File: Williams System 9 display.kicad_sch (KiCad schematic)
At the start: 30 parts, among them J101 Conn_01x02, J102 Conn_01x08, J103 Conn_01x08, J104 Conn_01x03, J105 Conn_01x04, J106 Conn_01x04, U101 74HC148, U102 74LV08A, U103 Pico, U104 74HC148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

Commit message: Make AKL available via personal component library for ease of integration
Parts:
- C101, C102, C103, C104, C105, C106, C107, C108: symbol PCM_Capacitor_US_AKL:C_0805 -> Capacitor_US_AKL:C_0805
- R101, R102, R103, R104, R105: symbol PCM_Resistor_US_AKL:R_0805 -> Resistor_US_AKL:R_0805
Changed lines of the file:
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@@
     )
   )
-  (symbol (lib_id "PCM_Capacitor_US_AKL:C_0805") (at 256.54 127 0) (unit 1)
+  (symbol (lib_id "Capacitor_US_AKL:C_0805") (at 256.54 127 0) (unit 1)
     (in_bom yes) (on_board yes) (dnp no) (fields_autoplaced)
     (property "Reference" "C108" (at 260.35 125.73 0)
@@
     )
   )
-  (symbol (lib_id "PCM_Resistor_US_AKL:R_0805") (at 255.27 90.17 0) (unit 1)
+  (symbol (lib_id "Resistor_US_AKL:R_0805") (at 255.27 90.17 0) (unit 1)
     (in_bom yes) (on_board yes) (dnp no)
     (property "Reference" "R102" (at 256.54 88.9 0)
@@
     )
   )
-  (symbol (lib_id "PCM_Capacitor_US_AKL:C_0805") (at 203.2 133.35 0) (mirror y) (unit 1)
+  (symbol (lib_id "Capacitor_US_AKL:C_0805") (at 203.2 133.35 0) (mirror y) (unit 1)
     (in_bom yes) (on_board yes) (dnp no)
     (property "Reference" "C107" (at 199.39 132.08 0)
@@
     )
   )
-  (symbol (lib_id "PCM_Resistor_US_AKL:R_0805") (at 257.81 64.77 90) (unit 1)
+  (symbol (lib_id "Resistor_US_AKL:R_0805") (at 257.81 64.77 90) (unit 1)
     (in_bom yes) (on_board yes) (dnp no)
     (property "Reference" "R105" (at 257.81 59.69 90)
@@
     )
   )
-  (symbol (lib_id "PCM_Capacitor_US_AKL:C_0805") (at 127 30.48 0) (unit 1)
+  (symbol (lib_id "Capacitor_US_AKL:C_0805") (at 127 30.48 0) (unit 1)
     (in_bom yes) (on_board yes) (dnp no)
     (property "Reference" "C102" (at 129.54 29.21 0)
@@
     )
   )
-  (symbol (lib_id "PCM_Resistor_US_AKL:R_0805") (at 257.81 73.66 90) (unit 1)
+  (symbol (lib_id "Resistor_US_AKL:R_0805") (at 257.81 73.66 90) (unit 1)
     (in_bom yes) (on_board yes) (dnp no)
     (property "Reference" "R104" (at 257.81 68.58 90)
@@
     )
   )
-  (symbol (lib_id "PCM_Capacitor_US_AKL:C_0805") (at 66.04 82.55 0) (unit 1)
+  (symbol (lib_id "Capacitor_US_AKL:C_0805") (at 66.04 82.55 0) (unit 1)
     (in_bom yes) (on_board yes) (dnp no)
     (property "Reference" "C103" (at 68.58 81.28 0)
@@
     )
   )
-  (symbol (lib_id "PCM_Capacitor_US_AKL:C_0805") (at 66.04 27.94 0) (unit 1)
+  (symbol (lib_id "Capacitor_US_AKL:C_0805") (at 66.04 27.94 0) (unit 1)
     (in_bom yes) (on_board yes) (dnp no)
     (property "Reference" "C101" (at 68.58 26.67 0)
@@
     )
   )
-  (symbol (lib_id "PCM_Capacitor_US_AKL:C_0805") (at 81.28 154.94 0) (unit 1)
+  (symbol (lib_id "Capacitor_US_AKL:C_0805") (at 81.28 154.94 0) (unit 1)
     (in_bom yes) (on_board yes) (dnp no) (fields_autoplaced)
     (property "Reference" "C106" (at 85.09 153.67 0)
@@
     )
   )
-  (symbol (lib_id "PCM_Capacitor_US_AKL:C_0805") (at 115.57 121.92 0) (unit 1)
+  (symbol (lib_id "Capacitor_US_AKL:C_0805") (at 115.57 121.92 0) (unit 1)
     (in_bom yes) (on_board yes) (dnp no)
     (property "Reference" "C104" (at 118.11 120.65 0)
@@
     )
   )
-  (symbol (lib_id "PCM_Resistor_US_AKL:R_0805") (at 257.81 78.74 90) (unit 1)
+  (symbol (lib_id "Resistor_US_AKL:R_0805") (at 257.81 78.74 90) (unit 1)
     (in_bom yes) (on_board yes) (dnp no)
     (property "Reference" "R103" (at 257.81 81.28 90)
@@
     )
   )
-  (symbol (lib_id "PCM_Resistor_US_AKL:R_0805") (at 264.16 93.98 0) (unit 1)
+  (symbol (lib_id "Resistor_US_AKL:R_0805") (at 264.16 93.98 0) (unit 1)
     (in_bom yes) (on_board yes) (dnp no)
     (property "Reference" "R101" (at 265.43 92.71 0)
@@
     )
   )
-  (symbol (lib_id "PCM_Capacitor_US_AKL:C_0805") (at 154.94 153.67 0) (unit 1)
+  (symbol (lib_id "Capacitor_US_AKL:C_0805") (at 154.94 153.67 0) (unit 1)
     (in_bom yes) (on_board yes) (dnp no) (fields_autoplaced)
     (property "Reference" "C105" (at 158.75 152.4 0)

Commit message: Address the remaining ERC violations
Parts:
- U107: footprint Package_TO_SOT_SMD_AKL:SOT-363_SC-70-6_BigPads -> Package_TO_SOT_SMD_AKL:SOT-363_SC-70-6_Handsoldering
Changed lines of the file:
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@@
   (junction (at 154.94 158.75) (diameter 0) (color 0 0 0 0)
+  )
+  (junction (at 130.81 25.4) (diameter 0) (color 0 0 0 0)
   )
   (junction (at 139.7 35.56) (diameter 0) (color 0 0 0 0)
@@
   (no_connect (at 223.52 104.14))
   (no_connect (at 143.51 173.99))
-  (wire (pts (xy 127 25.4) (xy 135.89 25.4))
+  (wire (pts (xy 127 25.4) (xy 130.81 25.4))
     (stroke (width 0) (type default))
   )
@@
   )
   (wire (pts (xy 123.19 27.94) (xy 123.19 35.56))
+    (stroke (width 0) (type default))
+  )
+  (wire (pts (xy 130.81 25.4) (xy 135.89 25.4))
     (stroke (width 0) (type default))
   )
@@
       (effects (font (size 1.27 1.27)))
     )
-    (property "Footprint" "Package_TO_SOT_SMD_AKL:SOT-363_SC-70-6_BigPads" (at 146.05 39.37 0)
+    (property "Footprint" "Package_TO_SOT_SMD_AKL:SOT-363_SC-70-6_Handsoldering" (at 146.05 39.37 0)
       (effects (font (size 1.27 1.27)) hide)
     )
@@
     (pin "2")
     (pin "3")
-    (pin "5")
     (pin "6")
     (pin "4")
+    (pin "5" (alternate "ST_{NA}"))
     (instances
       (project "Williams System 9 display"
@@
         )
       )
+    )
+  )
+  (symbol (lib_id "power:PWR_FLAG") (at 130.81 25.4 0) (unit 1)
+    (in_bom yes) (on_board yes) (dnp no) (fields_autoplaced)
+    (property "Reference" "#FLG0101" (at 130.81 23.495 0)
+      (effects (font (size 1.27 1.27)) hide)
+    )
+    (property "Value" "PWR_FLAG" (at 130.81 20.32 0)
+      (effects (font (size 1.27 1.27)) hide)
+    )
+    (property "Footprint" "" (at 130.81 25.4 0)
+      (effects (font (size 1.27 1.27)) hide)
+    )
+    (property "Datasheet" "~" (at 130.81 25.4 0)
+      (effects (font (size 1.27 1.27)) hide)
+    )
+    (pin "1")
+    (instances
+      (project "Williams System 9 display"
+        (path "/4315ddb4-8ca0-4300-a1f0-a77c526acaa2"
+          (reference "#FLG0101") (unit 1)
+        )
+      )

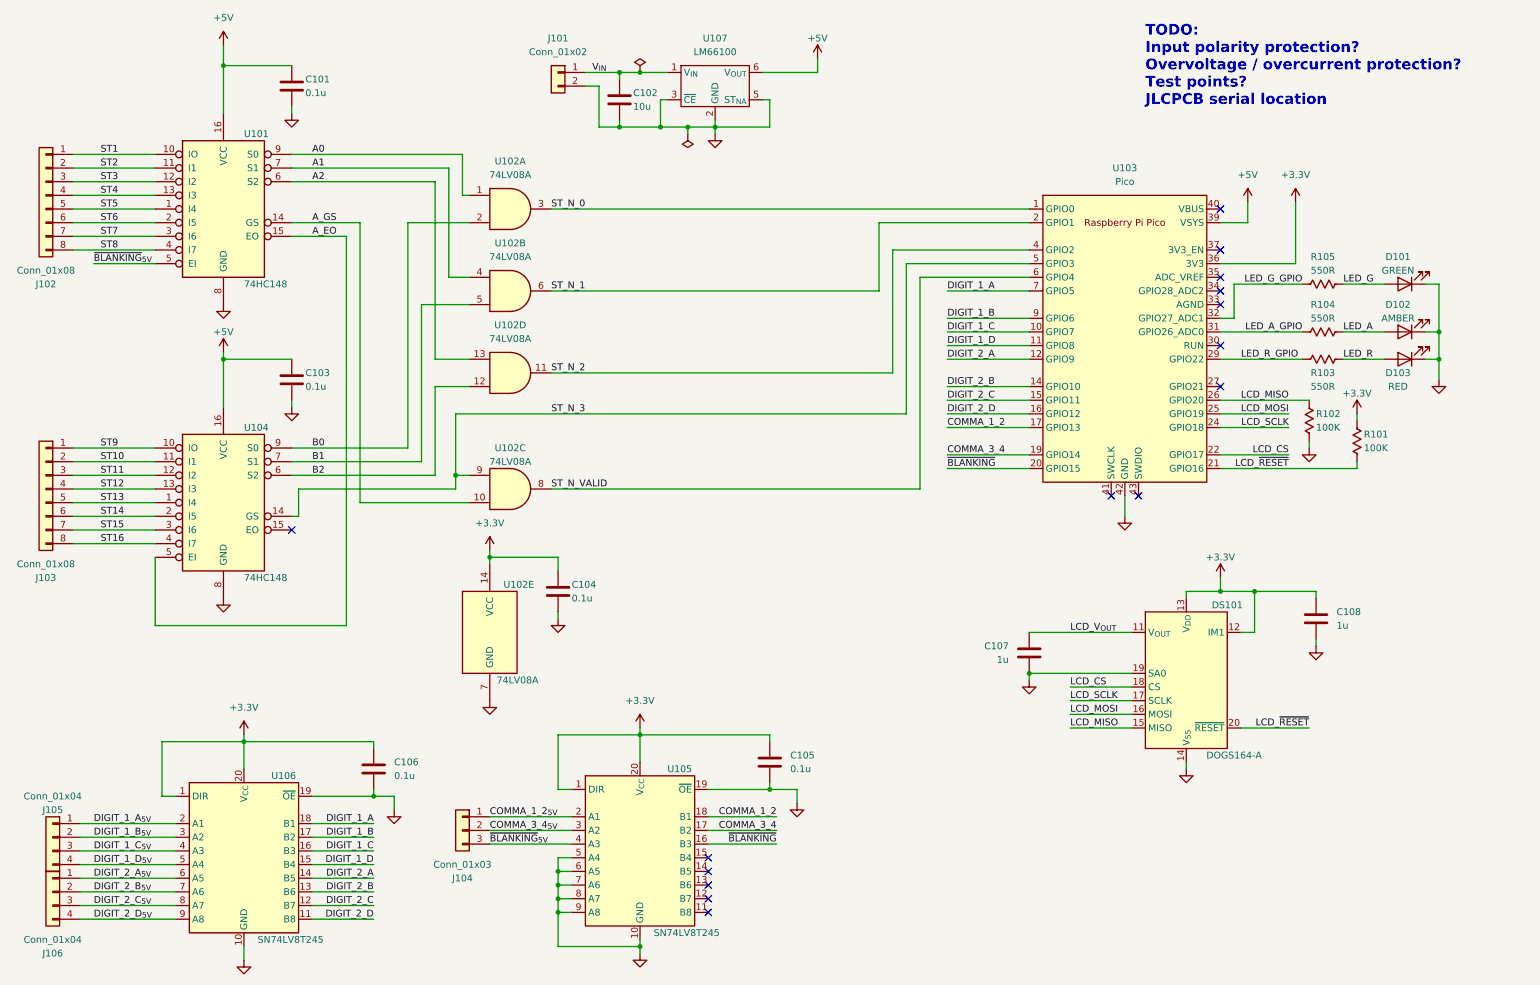
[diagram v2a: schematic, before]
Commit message: More informative silkscreen
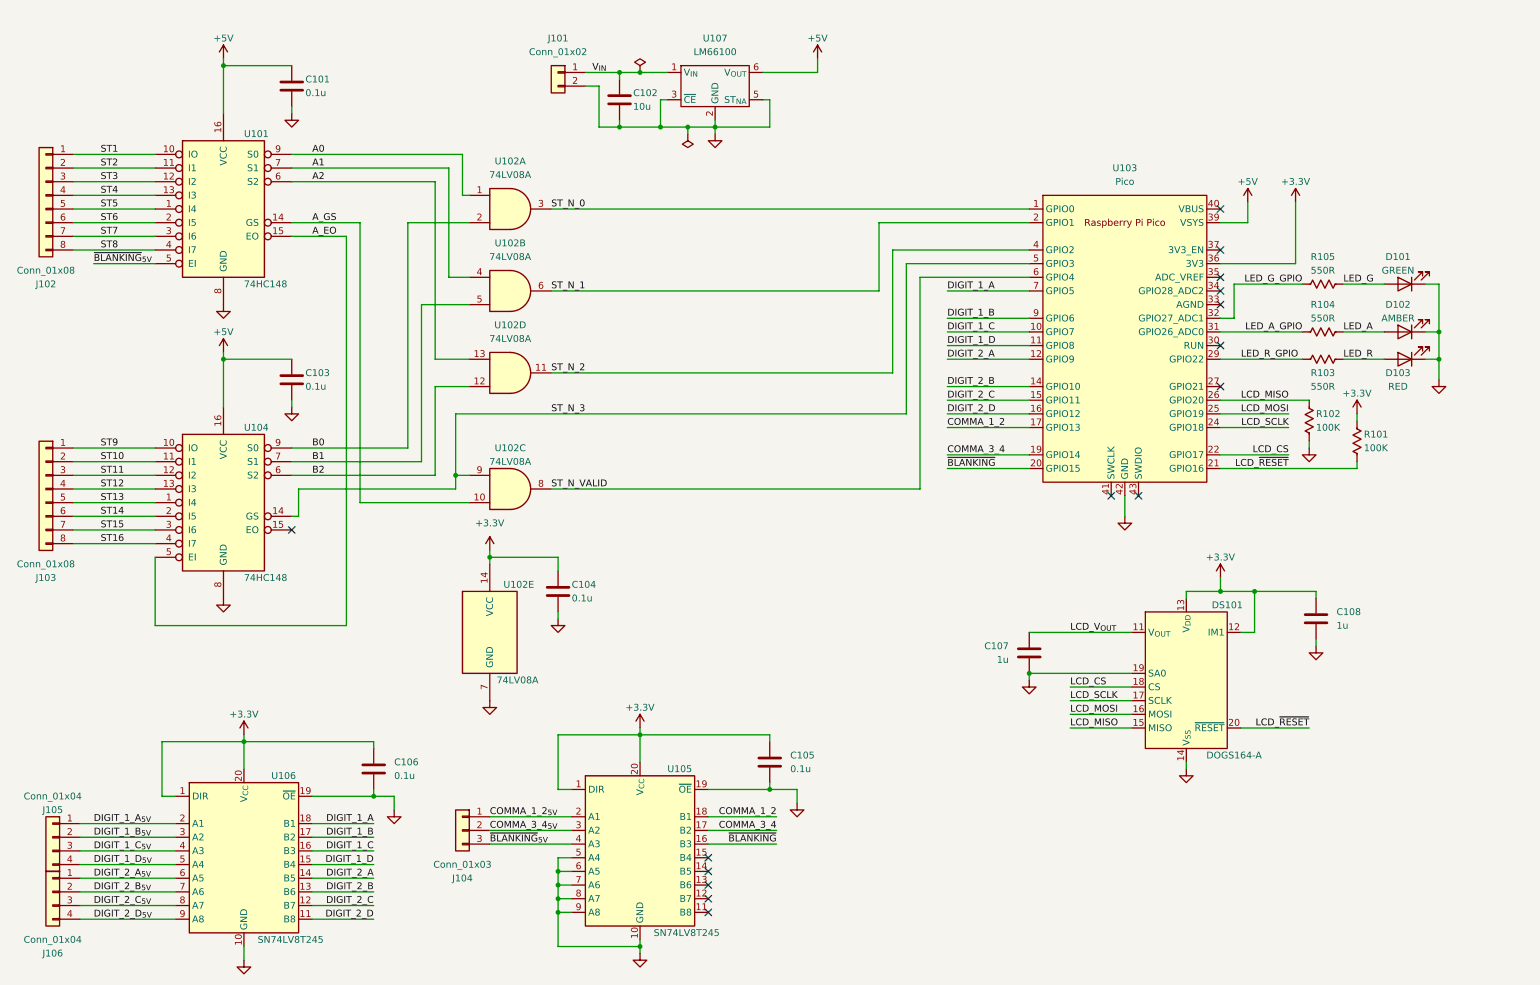
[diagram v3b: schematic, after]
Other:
- note removed: "TODO: Input polarity protection? Overvoltage / overcurrent protection? Test points? JLCPCB serial location"
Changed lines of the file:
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@@
     (stroke (width 0) (type default))
   )
-  (wire (pts (xy 53.34 20.32) (xy 53.34 24.13))
+  (wire (pts (xy 53.34 22.86) (xy 53.34 24.13))
     (stroke (width 0) (type default))
   )
@@
   (wire (pts (xy 90.17 97.79) (xy 90.17 68.58))
     (stroke (width 0) (type default))
-  )
-  (text "TODO:\nInput polarity protection?\nOvervoltage / overcurrent protection?\nTest points?\nJLCPCB serial location"
-    (at 224.79 31.75 0)
-    (effects (font (size 2 2) (thickness 0.4) bold) (justify left bottom))
   )
   (label "ST_N_0" (at 114.3 50.8 0) (fields_autoplaced)
@@
   )
   (symbol (lib_id "power:+3.3V") (at 130.81 147.32 0) (unit 1)
-    (in_bom yes) (on_board yes) (dnp no) (fields_autoplaced)
+    (in_bom yes) (on_board yes) (dnp no)
     (property "Reference" "#PWR0115" (at 130.81 151.13 0)
       (effects (font (size 1.27 1.27)) hide)
     )
-    (property "Value" "+3.3V" (at 130.81 142.24 0)
+    (property "Value" "+3.3V" (at 130.81 143.51 0)
       (effects (font (size 1.27 1.27)))
     )
@@
     )
   )
-  (symbol (lib_id "power:+5V") (at 53.34 20.32 0) (unit 1)
-    (in_bom yes) (on_board yes) (dnp no) (fields_autoplaced)
-    (property "Reference" "#PWR0101" (at 53.34 24.13 0)
-      (effects (font (size 1.27 1.27)) hide)
-    )
-    (property "Value" "+5V" (at 53.34 15.24 0)
-      (effects (font (size 1.27 1.27)))
-    )
-    (property "Footprint" "" (at 53.34 20.32 0)
-      (effects (font (size 1.27 1.27)) hide)
-    )
-    (property "Datasheet" "" (at 53.34 20.32 0)
+  (symbol (lib_id "power:+5V") (at 53.34 22.86 0) (unit 1)
+    (in_bom yes) (on_board yes) (dnp no)
+    (property "Reference" "#PWR0101" (at 53.34 26.67 0)
+      (effects (font (size 1.27 1.27)) hide)
+    )
+    (property "Value" "+5V" (at 53.34 19.05 0)
+      (effects (font (size 1.27 1.27)))
+    )
+    (property "Footprint" "" (at 53.34 22.86 0)
+      (effects (font (size 1.27 1.27)) hide)
+    )
+    (property "Datasheet" "" (at 53.34 22.86 0)
       (effects (font (size 1.27 1.27)) hide)
     )
@@
   )
   (symbol (lib_id "power:+5V") (at 243.84 49.53 0) (unit 1)
-    (in_bom yes) (on_board yes) (dnp no) (fields_autoplaced)
+    (in_bom yes) (on_board yes) (dnp no)
     (property "Reference" "#PWR0105" (at 243.84 53.34 0)
       (effects (font (size 1.27 1.27)) hide)
     )
-    (property "Value" "+5V" (at 243.84 44.45 0)
+    (property "Value" "+5V" (at 243.84 45.72 0)
       (effects (font (size 1.27 1.27)))
     )
@@
   )
   (symbol (lib_id "power:+3.3V") (at 252.73 49.53 0) (unit 1)
-    (in_bom yes) (on_board yes) (dnp no) (fields_autoplaced)
+    (in_bom yes) (on_board yes) (dnp no)
     (property "Reference" "#PWR0106" (at 252.73 53.34 0)
       (effects (font (size 1.27 1.27)) hide)
     )
-    (property "Value" "+3.3V" (at 252.73 44.45 0)
+    (property "Value" "+3.3V" (at 252.73 45.72 0)
       (effects (font (size 1.27 1.27)))
     )
@@
   )
   (symbol (lib_id "power:+3.3V") (at 57.15 148.59 0) (unit 1)
-    (in_bom yes) (on_board yes) (dnp no) (fields_autoplaced)
+    (in_bom yes) (on_board yes) (dnp no)
     (property "Reference" "#PWR0116" (at 57.15 152.4 0)
       (effects (font (size 1.27 1.27)) hide)
     )
-    (property "Value" "+3.3V" (at 57.15 143.51 0)
-      (effects (font (size 1.27 1.27)))
-    )
+    (property "Value" "+3.3V" (at 57.15 144.78 0)
+      (effects (font (size 1.27 1.27)))
+    )

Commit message: Don't use BLANKING as enable signal for priority encoder since it is of the wrong polarity
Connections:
- net GND: now also U101.5 (EI)
- net ~{BLANKING}_{5V}: no longer U101.5 (EI)
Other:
- note added: "TODO: Use ~{BLANKING} to enable the priority encoder rather than tying EI directly to ground."
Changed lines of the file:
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@@
   (junction (at 130.81 25.4) (diameter 0) (color 0 0 0 0)
+  )
+  (junction (at 53.34 68.58) (diameter 0) (color 0 0 0 0)
   )
   (junction (at 139.7 35.56) (diameter 0) (color 0 0 0 0)
@@
     (stroke (width 0) (type default))
   )
+  (wire (pts (xy 39.37 60.96) (xy 40.64 60.96))
+    (stroke (width 0) (type default))
+  )
   (wire (pts (xy 241.3 64.77) (xy 254 64.77))
     (stroke (width 0) (type default))
@@
     (stroke (width 0) (type default))
   )
+  (wire (pts (xy 53.34 68.58) (xy 39.37 68.58))
+    (stroke (width 0) (type default))
+  )
   (wire (pts (xy 114.3 102.87) (xy 182.88 102.87))
     (stroke (width 0) (type default))
@@
     (stroke (width 0) (type default))
   )
+  (wire (pts (xy 39.37 68.58) (xy 39.37 60.96))
+    (stroke (width 0) (type default))
+  )
   (wire (pts (xy 232.41 121.92) (xy 232.41 123.19))
     (stroke (width 0) (type default))
@@
     (stroke (width 0) (type default))
   )
-  (wire (pts (xy 29.21 60.96) (xy 40.64 60.96))
-    (stroke (width 0) (type default))
-  )
   (wire (pts (xy 238.76 88.9) (xy 251.46 88.9))
     (stroke (width 0) (type default))
@@
   (wire (pts (xy 90.17 97.79) (xy 90.17 68.58))
     (stroke (width 0) (type default))
+  )
+  (text "TODO:\nUse ~{BLANKING} to enable the priority\nencoder rather than tying EI directly\nto ground."
+    (at 17.78 77.47 0)
+    (effects (font (face "KiCad Font") (size 1 1)) (justify left bottom))
   )
   (label "ST_N_0" (at 114.3 50.8 0) (fields_autoplaced)
@@
     (effects (font (size 1.27 1.27)) (justify left bottom))
   )
-  (label "~{BLANKING}_{5V}" (at 29.21 60.96 0) (fields_autoplaced)
-    (effects (font (size 1.27 1.27)) (justify left bottom))
-  )
